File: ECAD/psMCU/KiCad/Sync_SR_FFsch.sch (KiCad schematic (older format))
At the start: 8 parts, among them U101 SN74LVC1G32DCK, U102 SN74LVC1G08DCK, U114 SN74LVC1G175DCK, U96 SN74LVC1G04DCK

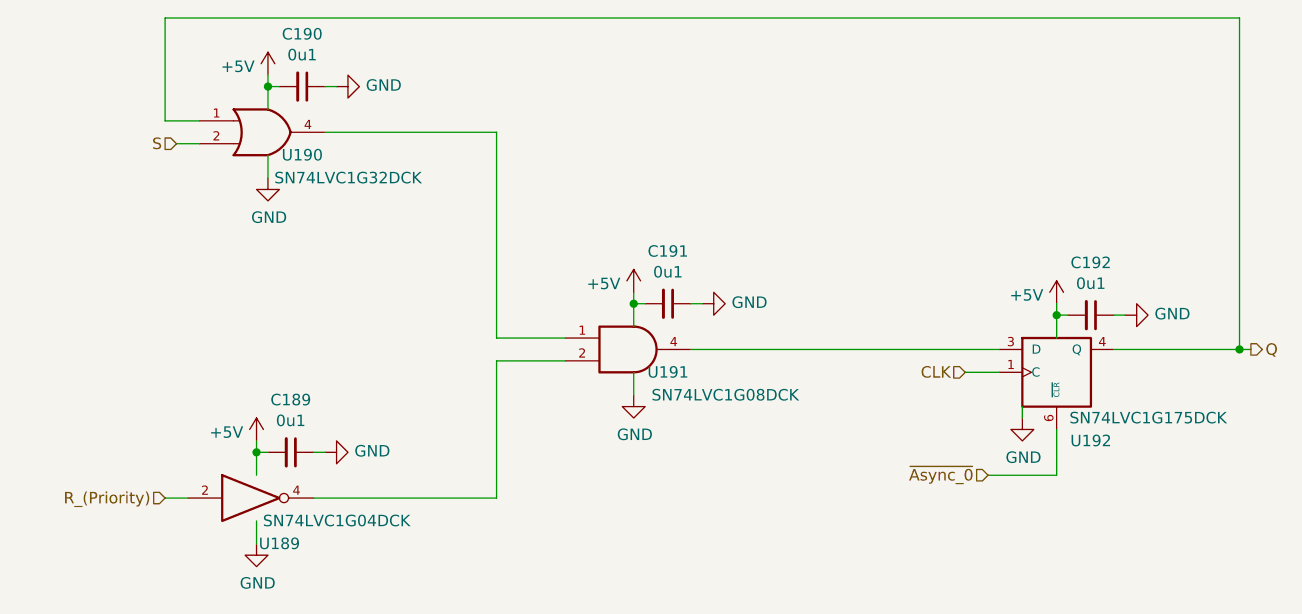
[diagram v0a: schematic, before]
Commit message: Sch: Fixed SYS1 Register
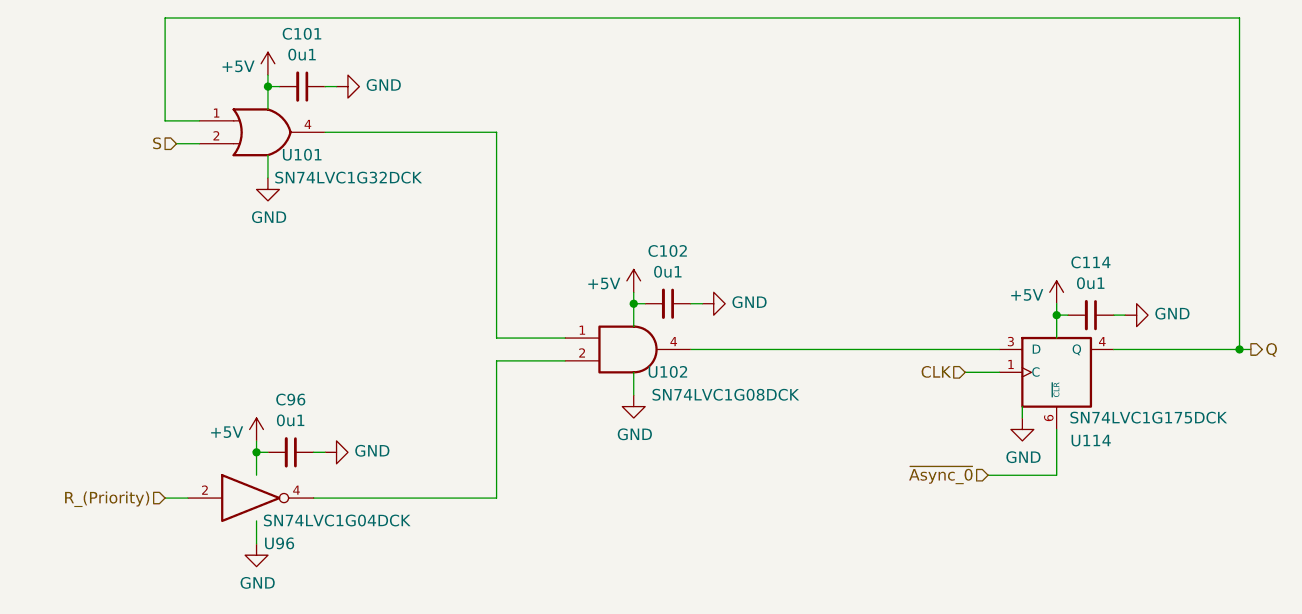
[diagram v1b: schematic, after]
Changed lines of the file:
@@
 $Descr A4 11693 8268
 encoding utf-8
-Sheet 21 97
+Sheet 20 97
 Title "psMCU"
 Date "2022-02-13"
@@
 AR Path="/60E33DBC/5FD12DEC/60B2DD5B/60B01E14" Ref="#PWR0412"  Part="1"
 AR Path="/60E33DBC/5FD12DEC/60B2E59A/60B01E14" Ref="#PWR0443"  Part="1"
-F 0 "#PWR0443" H 6700 3350 50  0001 C CNN
+F 0 "#PWR0375" H 6700 3350 50  0001 C CNN
 F 1 "GND" H 6705 3427 50  0000 C CNN
 F 2 "" H 6700 3600 50  0001 C CNN
@@
 AR Path="/60E33DBC/5FD12DEC/60B2DD5B/60B01E1A" Ref="#PWR0416"  Part="1"
 AR Path="/60E33DBC/5FD12DEC/60B2E59A/60B01E1A" Ref="#PWR0445"  Part="1"
-F 0 "#PWR0445" H 7150 2900 50  0001 C CNN
+F 0 "#PWR0385" H 7150 2900 50  0001 C CNN
 F 1 "GND" V 7155 3022 50  0000 R CNN
 F 2 "" H 7150 3150 50  0001 C CNN
@@
 AR Path="/60E33DBC/5FD12DEC/60B2DD5B/60B01E21" Ref="C188"  Part="1"
 AR Path="/60E33DBC/5FD12DEC/60B2E59A/60B01E21" Ref="C192"  Part="1"
-F 0 "C192" V 6771 3150 50  0000 C CNN
+F 0 "C114" V 6771 3150 50  0000 C CNN
 F 1 "0u1" V 6862 3150 50  0000 C CNN
 F 2 "NoRef_Footprints:C_0603_1608Metric_NoRef" H 7000 3150 50  0001 C CNN
@@
 AR Path="/60E33DBC/5FD12DEC/60B2DD5B/60B01E27" Ref="#PWR0415"  Part="1"
 AR Path="/60E33DBC/5FD12DEC/60B2E59A/60B01E27" Ref="#PWR0444"  Part="1"
-F 0 "#PWR0444" H 6850 2950 50  0001 C CNN
+F 0 "#PWR0380" H 6850 2950 50  0001 C CNN
 F 1 "+5V" H 6792 3137 50  0000 R CNN
 F 2 "" H 6850 3100 50  0001 C CNN
@@
 AR Path="/60E33DBC/5FD12DEC/60B2DD5B/60B01E61" Ref="U188"  Part="1"
 AR Path="/60E33DBC/5FD12DEC/60B2E59A/60B01E61" Ref="U192"  Part="1"
-F 0 "U192" H 7000 3100 50  0000 C CNN
+F 0 "U114" H 7000 3100 50  0000 C CNN
 F 1 "SN74LVC1G175DCK" H 7250 3200 50  0000 C CNN
 F 2 "Package_TO_SOT_SMD:SOT-363_SC-70-6" H 6850 3400 50  0001 C CNN
@@
 AR Path="/60E33DBC/5FD12DEC/60B2DD5B/60B07E89" Ref="U152"  Part="1"
 AR Path="/60E33DBC/5FD12DEC/60B2E59A/60B07E89" Ref="U191"  Part="1"
-F 0 "U191" H 5150 3200 50  0000 C CNN
+F 0 "U102" H 5150 3200 50  0000 C CNN
 F 1 "SN74LVC1G08DCK" H 5400 3100 50  0000 C CNN
 F 2 "Package_TO_SOT_SMD:SOT-353_SC-70-5" H 5000 3300 50  0001 C CNN
@@
 AR Path="/60E33DBC/5FD12DEC/60B2DD5B/60B07E8F" Ref="#PWR0409"  Part="1"
 AR Path="/60E33DBC/5FD12DEC/60B2E59A/60B07E8F" Ref="#PWR0441"  Part="1"
-F 0 "#PWR0441" H 5000 3250 50  0001 C CNN
+F 0 "#PWR0361" H 5000 3250 50  0001 C CNN
 F 1 "GND" H 5005 3327 50  0000 C CNN
 F 2 "" H 5000 3500 50  0001 C CNN
@@
 AR Path="/60E33DBC/5FD12DEC/60B2DD5B/60B07E97" Ref="#PWR0408"  Part="1"
 AR Path="/60E33DBC/5FD12DEC/60B2E59A/60B07E97" Ref="#PWR0440"  Part="1"
-F 0 "#PWR0440" H 5000 2900 50  0001 C CNN
+F 0 "#PWR0360" H 5000 2900 50  0001 C CNN
 F 1 "+5V" H 4942 3087 50  0000 R CNN
 F 2 "" H 5000 3050 50  0001 C CNN
@@
 AR Path="/60E33DBC/5FD12DEC/60B2DD5B/60B07E9D" Ref="C151"  Part="1"
 AR Path="/60E33DBC/5FD12DEC/60B2E59A/60B07E9D" Ref="C191"  Part="1"
-F 0 "C191" V 4921 3100 50  0000 C CNN
+F 0 "C102" V 4921 3100 50  0000 C CNN
 F 1 "0u1" V 5012 3100 50  0000 C CNN
 F 2 "NoRef_Footprints:C_0603_1608Metric_NoRef" H 5150 3100 50  0001 C CNN
@@
 AR Path="/60E33DBC/5FD12DEC/60B2DD5B/60B07EA6" Ref="#PWR0411"  Part="1"
 AR Path="/60E33DBC/5FD12DEC/60B2E59A/60B07EA6" Ref="#PWR0442"  Part="1"
-F 0 "#PWR0442" H 5300 2850 50  0001 C CNN
+F 0 "#PWR0373" H 5300 2850 50  0001 C CNN
 F 1 "GND" V 5305 2972 50  0000 R CNN
 F 2 "" H 5300 3100 50  0001 C CNN
@@
 AR Path="/60E33DBC/5FD12DEC/60B2DD5B/60B07EAD" Ref="U150"  Part="1"
 AR Path="/60E33DBC/5FD12DEC/60B2E59A/60B07EAD" Ref="U190"  Part="1"
-F 0 "U190" H 3550 2250 50  0000 C CNN
+F 0 "U101" H 3550 2250 50  0000 C CNN
 F 1 "SN74LVC1G32DCK" H 3750 2150 50  0000 C CNN
 F 2 "Package_TO_SOT_SMD:SOT-353_SC-70-5" H 3400 2350 50  0001 C CNN
@@
 AR Path="/60E33DBC/5FD12DEC/60B2DD5B/60B07EB3" Ref="#PWR0400"  Part="1"
 AR Path="/60E33DBC/5FD12DEC/60B2E59A/60B07EB3" Ref="#PWR0427"  Part="1"
-F 0 "#PWR0427" H 3400 2300 50  0001 C CNN
+F 0 "#PWR0355" H 3400 2300 50  0001 C CNN
 F 1 "GND" H 3405 2377 50  0000 C CNN
 F 2 "" H 3400 2550 50  0001 C CNN
@@
 AR Path="/60E33DBC/5FD12DEC/60B2DD5B/60B07EBB" Ref="#PWR0399"  Part="1"
 AR Path="/60E33DBC/5FD12DEC/60B2E59A/60B07EBB" Ref="#PWR0421"  Part="1"
-F 0 "#PWR0421" H 3400 1950 50  0001 C CNN
+F 0 "#PWR0354" H 3400 1950 50  0001 C CNN
 F 1 "+5V" H 3342 2137 50  0000 R CNN
 F 2 "" H 3400 2100 50  0001 C CNN
@@
 AR Path="/60E33DBC/5FD12DEC/60B2DD5B/60B07EC1" Ref="C150"  Part="1"
 AR Path="/60E33DBC/5FD12DEC/60B2E59A/60B07EC1" Ref="C190"  Part="1"
-F 0 "C190" V 3321 2150 50  0000 C CNN
+F 0 "C101" V 3321 2150 50  0000 C CNN
 F 1 "0u1" V 3412 2150 50  0000 C CNN
 F 2 "NoRef_Footprints:C_0603_1608Metric_NoRef" H 3550 2150 50  0001 C CNN
@@
 AR Path="/60E33DBC/5FD12DEC/60B2DD5B/60B07ECA" Ref="#PWR0407"  Part="1"
 AR Path="/60E33DBC/5FD12DEC/60B2E59A/60B07ECA" Ref="#PWR0437"  Part="1"
-F 0 "#PWR0437" H 3700 1900 50  0001 C CNN
+F 0 "#PWR0357" H 3700 1900 50  0001 C CNN
 F 1 "GND" V 3705 2022 50  0000 R CNN
 F 2 "" H 3700 2150 50  0001 C CNN
@@
 AR Path="/60E33DBC/5FD12DEC/60B2DD5B/60B07ED1" Ref="U115"  Part="1"
 AR Path="/60E33DBC/5FD12DEC/60B2E59A/60B07ED1" Ref="U189"  Part="1"
-F 0 "U189" H 3450 3750 50  0000 C CNN
+F 0 "U96" H 3450 3750 50  0000 C CNN
 F 1 "SN74LVC1G04DCK" H 3700 3850 50  0000 C CNN
 F 2 "Package_TO_SOT_SMD:SOT-353_SC-70-5" H 3350 3950 50  0001 C CNN
@@
 AR Path="/60E33DBC/5FD12DEC/60B2DD5B/60B07ED8" Ref="#PWR0386"  Part="1"
 AR Path="/60E33DBC/5FD12DEC/60B2E59A/60B07ED8" Ref="#PWR0417"  Part="1"
-F 0 "#PWR0417" H 3350 3550 50  0001 C CNN
+F 0 "#PWR0352" H 3350 3550 50  0001 C CNN
 F 1 "+5V" H 3292 3737 50  0000 R CNN
 F 2 "" H 3350 3700 50  0001 C CNN
@@
 AR Path="/60E33DBC/5FD12DEC/60B2DD5B/60B07EDE" Ref="C115"  Part="1"
 AR Path="/60E33DBC/5FD12DEC/60B2E59A/60B07EDE" Ref="C189"  Part="1"
-F 0 "C189" V 3271 3750 50  0000 C CNN
+F 0 "C96" V 3271 3750 50  0000 C CNN
 F 1 "0u1" V 3362 3750 50  0000 C CNN
 F 2 "NoRef_Footprints:C_0603_1608Metric_NoRef" H 3500 3750 50  0001 C CNN
@@
 AR Path="/60E33DBC/5FD12DEC/60B2DD5B/60B07EE7" Ref="#PWR0406"  Part="1"
 AR Path="/60E33DBC/5FD12DEC/60B2E59A/60B07EE7" Ref="#PWR0436"  Part="1"
-F 0 "#PWR0436" H 3650 3500 50  0001 C CNN
+F 0 "#PWR0356" H 3650 3500 50  0001 C CNN
 F 1 "GND" V 3655 3622 50  0000 R CNN
 F 2 "" H 3650 3750 50  0001 C CNN
@@
 AR Path="/60E33DBC/5FD12DEC/60B2DD5B/60B07EEE" Ref="#PWR0390"  Part="1"
 AR Path="/60E33DBC/5FD12DEC/60B2E59A/60B07EEE" Ref="#PWR0419"  Part="1"
-F 0 "#PWR0419" H 3350 3900 50  0001 C CNN
+F 0 "#PWR0353" H 3350 3900 50  0001 C CNN
 F 1 "GND" H 3355 3977 50  0000 C CNN
 F 2 "" H 3350 4150 50  0001 C CNN

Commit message: Sch: Changed LDD behaviour (now is literal+b)
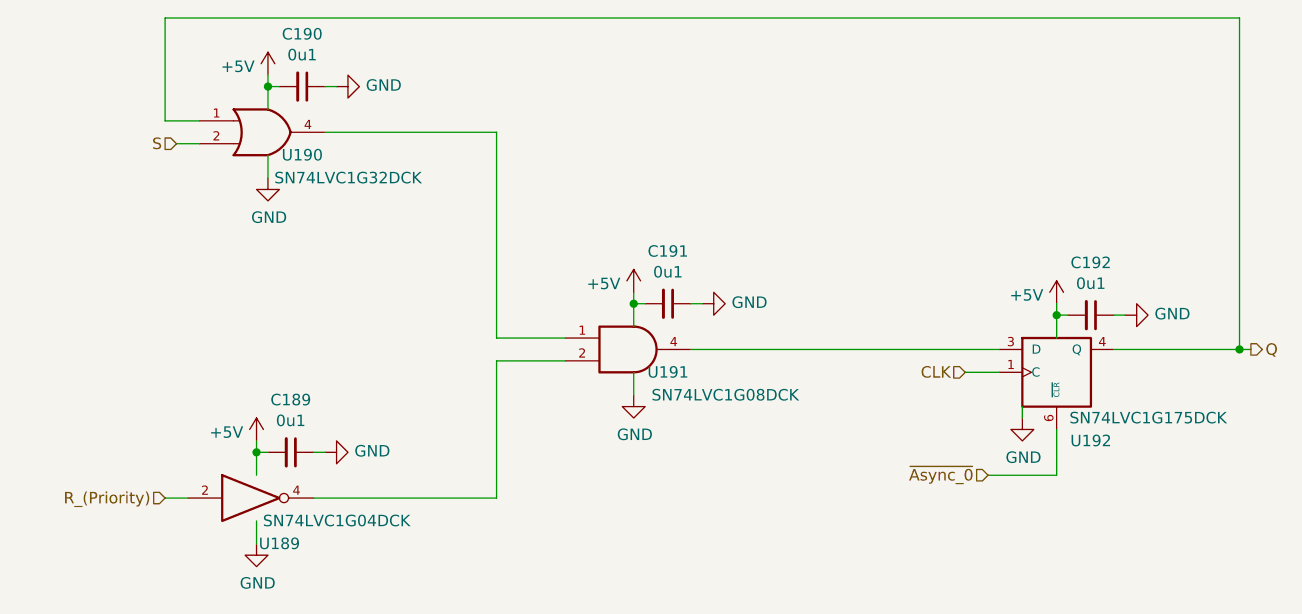
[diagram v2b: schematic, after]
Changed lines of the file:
@@
 $Descr A4 11693 8268
 encoding utf-8
-Sheet 20 97
+Sheet 22 97
 Title "psMCU"
 Date "2022-02-13"
@@
 AR Path="/60E33DBC/5FD12DEC/60B2DD5B/60B01E14" Ref="#PWR0412"  Part="1"
 AR Path="/60E33DBC/5FD12DEC/60B2E59A/60B01E14" Ref="#PWR0443"  Part="1"
-F 0 "#PWR0375" H 6700 3350 50  0001 C CNN
+F 0 "#PWR0443" H 6700 3350 50  0001 C CNN
 F 1 "GND" H 6705 3427 50  0000 C CNN
 F 2 "" H 6700 3600 50  0001 C CNN
@@
 AR Path="/60E33DBC/5FD12DEC/60B2DD5B/60B01E1A" Ref="#PWR0416"  Part="1"
 AR Path="/60E33DBC/5FD12DEC/60B2E59A/60B01E1A" Ref="#PWR0445"  Part="1"
-F 0 "#PWR0385" H 7150 2900 50  0001 C CNN
+F 0 "#PWR0445" H 7150 2900 50  0001 C CNN
 F 1 "GND" V 7155 3022 50  0000 R CNN
 F 2 "" H 7150 3150 50  0001 C CNN
@@
 AR Path="/60E33DBC/5FD12DEC/60B2DD5B/60B01E21" Ref="C188"  Part="1"
 AR Path="/60E33DBC/5FD12DEC/60B2E59A/60B01E21" Ref="C192"  Part="1"
-F 0 "C114" V 6771 3150 50  0000 C CNN
+F 0 "C192" V 6771 3150 50  0000 C CNN
 F 1 "0u1" V 6862 3150 50  0000 C CNN
 F 2 "NoRef_Footprints:C_0603_1608Metric_NoRef" H 7000 3150 50  0001 C CNN
@@
 AR Path="/60E33DBC/5FD12DEC/60B2DD5B/60B01E27" Ref="#PWR0415"  Part="1"
 AR Path="/60E33DBC/5FD12DEC/60B2E59A/60B01E27" Ref="#PWR0444"  Part="1"
-F 0 "#PWR0380" H 6850 2950 50  0001 C CNN
+F 0 "#PWR0444" H 6850 2950 50  0001 C CNN
 F 1 "+5V" H 6792 3137 50  0000 R CNN
 F 2 "" H 6850 3100 50  0001 C CNN
@@
 AR Path="/60E33DBC/5FD12DEC/60B2DD5B/60B01E61" Ref="U188"  Part="1"
 AR Path="/60E33DBC/5FD12DEC/60B2E59A/60B01E61" Ref="U192"  Part="1"
-F 0 "U114" H 7000 3100 50  0000 C CNN
+F 0 "U192" H 7000 3100 50  0000 C CNN
 F 1 "SN74LVC1G175DCK" H 7250 3200 50  0000 C CNN
 F 2 "Package_TO_SOT_SMD:SOT-363_SC-70-6" H 6850 3400 50  0001 C CNN
@@
 AR Path="/60E33DBC/5FD12DEC/60B2DD5B/60B07E89" Ref="U152"  Part="1"
 AR Path="/60E33DBC/5FD12DEC/60B2E59A/60B07E89" Ref="U191"  Part="1"
-F 0 "U102" H 5150 3200 50  0000 C CNN
+F 0 "U191" H 5150 3200 50  0000 C CNN
 F 1 "SN74LVC1G08DCK" H 5400 3100 50  0000 C CNN
 F 2 "Package_TO_SOT_SMD:SOT-353_SC-70-5" H 5000 3300 50  0001 C CNN
@@
 AR Path="/60E33DBC/5FD12DEC/60B2DD5B/60B07E8F" Ref="#PWR0409"  Part="1"
 AR Path="/60E33DBC/5FD12DEC/60B2E59A/60B07E8F" Ref="#PWR0441"  Part="1"
-F 0 "#PWR0361" H 5000 3250 50  0001 C CNN
+F 0 "#PWR0441" H 5000 3250 50  0001 C CNN
 F 1 "GND" H 5005 3327 50  0000 C CNN
 F 2 "" H 5000 3500 50  0001 C CNN
@@
 AR Path="/60E33DBC/5FD12DEC/60B2DD5B/60B07E97" Ref="#PWR0408"  Part="1"
 AR Path="/60E33DBC/5FD12DEC/60B2E59A/60B07E97" Ref="#PWR0440"  Part="1"
-F 0 "#PWR0360" H 5000 2900 50  0001 C CNN
+F 0 "#PWR0440" H 5000 2900 50  0001 C CNN
 F 1 "+5V" H 4942 3087 50  0000 R CNN
 F 2 "" H 5000 3050 50  0001 C CNN
@@
 AR Path="/60E33DBC/5FD12DEC/60B2DD5B/60B07E9D" Ref="C151"  Part="1"
 AR Path="/60E33DBC/5FD12DEC/60B2E59A/60B07E9D" Ref="C191"  Part="1"
-F 0 "C102" V 4921 3100 50  0000 C CNN
+F 0 "C191" V 4921 3100 50  0000 C CNN
 F 1 "0u1" V 5012 3100 50  0000 C CNN
 F 2 "NoRef_Footprints:C_0603_1608Metric_NoRef" H 5150 3100 50  0001 C CNN
@@
 AR Path="/60E33DBC/5FD12DEC/60B2DD5B/60B07EA6" Ref="#PWR0411"  Part="1"
 AR Path="/60E33DBC/5FD12DEC/60B2E59A/60B07EA6" Ref="#PWR0442"  Part="1"
-F 0 "#PWR0373" H 5300 2850 50  0001 C CNN
+F 0 "#PWR0442" H 5300 2850 50  0001 C CNN
 F 1 "GND" V 5305 2972 50  0000 R CNN
 F 2 "" H 5300 3100 50  0001 C CNN
@@
 AR Path="/60E33DBC/5FD12DEC/60B2DD5B/60B07EAD" Ref="U150"  Part="1"
 AR Path="/60E33DBC/5FD12DEC/60B2E59A/60B07EAD" Ref="U190"  Part="1"
-F 0 "U101" H 3550 2250 50  0000 C CNN
+F 0 "U190" H 3550 2250 50  0000 C CNN
 F 1 "SN74LVC1G32DCK" H 3750 2150 50  0000 C CNN
 F 2 "Package_TO_SOT_SMD:SOT-353_SC-70-5" H 3400 2350 50  0001 C CNN
@@
 AR Path="/60E33DBC/5FD12DEC/60B2DD5B/60B07EB3" Ref="#PWR0400"  Part="1"
 AR Path="/60E33DBC/5FD12DEC/60B2E59A/60B07EB3" Ref="#PWR0427"  Part="1"
-F 0 "#PWR0355" H 3400 2300 50  0001 C CNN
+F 0 "#PWR0427" H 3400 2300 50  0001 C CNN
 F 1 "GND" H 3405 2377 50  0000 C CNN
 F 2 "" H 3400 2550 50  0001 C CNN
@@
 AR Path="/60E33DBC/5FD12DEC/60B2DD5B/60B07EBB" Ref="#PWR0399"  Part="1"
 AR Path="/60E33DBC/5FD12DEC/60B2E59A/60B07EBB" Ref="#PWR0421"  Part="1"
-F 0 "#PWR0354" H 3400 1950 50  0001 C CNN
+F 0 "#PWR0421" H 3400 1950 50  0001 C CNN
 F 1 "+5V" H 3342 2137 50  0000 R CNN
 F 2 "" H 3400 2100 50  0001 C CNN
@@
 AR Path="/60E33DBC/5FD12DEC/60B2DD5B/60B07EC1" Ref="C150"  Part="1"
 AR Path="/60E33DBC/5FD12DEC/60B2E59A/60B07EC1" Ref="C190"  Part="1"
-F 0 "C101" V 3321 2150 50  0000 C CNN
+F 0 "C190" V 3321 2150 50  0000 C CNN
 F 1 "0u1" V 3412 2150 50  0000 C CNN
 F 2 "NoRef_Footprints:C_0603_1608Metric_NoRef" H 3550 2150 50  0001 C CNN
@@
 AR Path="/60E33DBC/5FD12DEC/60B2DD5B/60B07ECA" Ref="#PWR0407"  Part="1"
 AR Path="/60E33DBC/5FD12DEC/60B2E59A/60B07ECA" Ref="#PWR0437"  Part="1"
-F 0 "#PWR0357" H 3700 1900 50  0001 C CNN
+F 0 "#PWR0437" H 3700 1900 50  0001 C CNN
 F 1 "GND" V 3705 2022 50  0000 R CNN
 F 2 "" H 3700 2150 50  0001 C CNN
@@
 AR Path="/60E33DBC/5FD12DEC/60B2DD5B/60B07ED1" Ref="U115"  Part="1"
 AR Path="/60E33DBC/5FD12DEC/60B2E59A/60B07ED1" Ref="U189"  Part="1"
-F 0 "U96" H 3450 3750 50  0000 C CNN
+F 0 "U189" H 3450 3750 50  0000 C CNN
 F 1 "SN74LVC1G04DCK" H 3700 3850 50  0000 C CNN
 F 2 "Package_TO_SOT_SMD:SOT-353_SC-70-5" H 3350 3950 50  0001 C CNN
@@
 AR Path="/60E33DBC/5FD12DEC/60B2DD5B/60B07ED8" Ref="#PWR0386"  Part="1"
 AR Path="/60E33DBC/5FD12DEC/60B2E59A/60B07ED8" Ref="#PWR0417"  Part="1"
-F 0 "#PWR0352" H 3350 3550 50  0001 C CNN
+F 0 "#PWR0417" H 3350 3550 50  0001 C CNN
 F 1 "+5V" H 3292 3737 50  0000 R CNN
 F 2 "" H 3350 3700 50  0001 C CNN
@@
 AR Path="/60E33DBC/5FD12DEC/60B2DD5B/60B07EDE" Ref="C115"  Part="1"
 AR Path="/60E33DBC/5FD12DEC/60B2E59A/60B07EDE" Ref="C189"  Part="1"
-F 0 "C96" V 3271 3750 50  0000 C CNN
+F 0 "C189" V 3271 3750 50  0000 C CNN
 F 1 "0u1" V 3362 3750 50  0000 C CNN
 F 2 "NoRef_Footprints:C_0603_1608Metric_NoRef" H 3500 3750 50  0001 C CNN
@@
 AR Path="/60E33DBC/5FD12DEC/60B2DD5B/60B07EE7" Ref="#PWR0406"  Part="1"
 AR Path="/60E33DBC/5FD12DEC/60B2E59A/60B07EE7" Ref="#PWR0436"  Part="1"
-F 0 "#PWR0356" H 3650 3500 50  0001 C CNN
+F 0 "#PWR0436" H 3650 3500 50  0001 C CNN
 F 1 "GND" V 3655 3622 50  0000 R CNN
 F 2 "" H 3650 3750 50  0001 C CNN
@@
 AR Path="/60E33DBC/5FD12DEC/60B2DD5B/60B07EEE" Ref="#PWR0390"  Part="1"
 AR Path="/60E33DBC/5FD12DEC/60B2E59A/60B07EEE" Ref="#PWR0419"  Part="1"
-F 0 "#PWR0353" H 3350 3900 50  0001 C CNN
+F 0 "#PWR0419" H 3350 3900 50  0001 C CNN
 F 1 "GND" H 3355 3977 50  0000 C CNN
 F 2 "" H 3350 4150 50  0001 C CNN
